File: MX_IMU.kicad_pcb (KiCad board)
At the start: 4 copper layers, 40 x 36 mm, 50 parts, among them J1 CAN, J2 USART, J401 SWD, SW1 SW_SPST, U1 ld39150dt33-r, U2 ICM-42688-P, U200 STM32F405RGT6, U4 AT24C256, U6 TJA1051T/3, Y200 16MHz

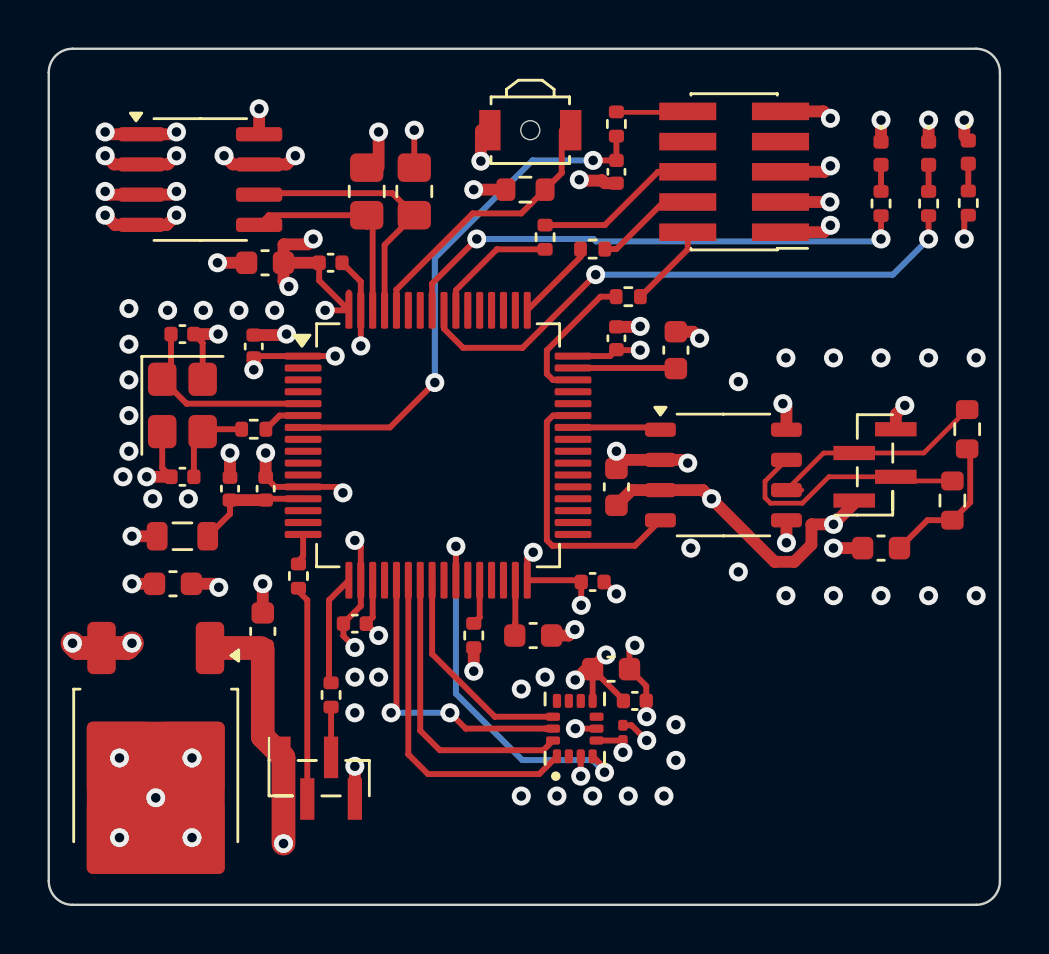
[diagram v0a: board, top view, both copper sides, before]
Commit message: add usb and clean up
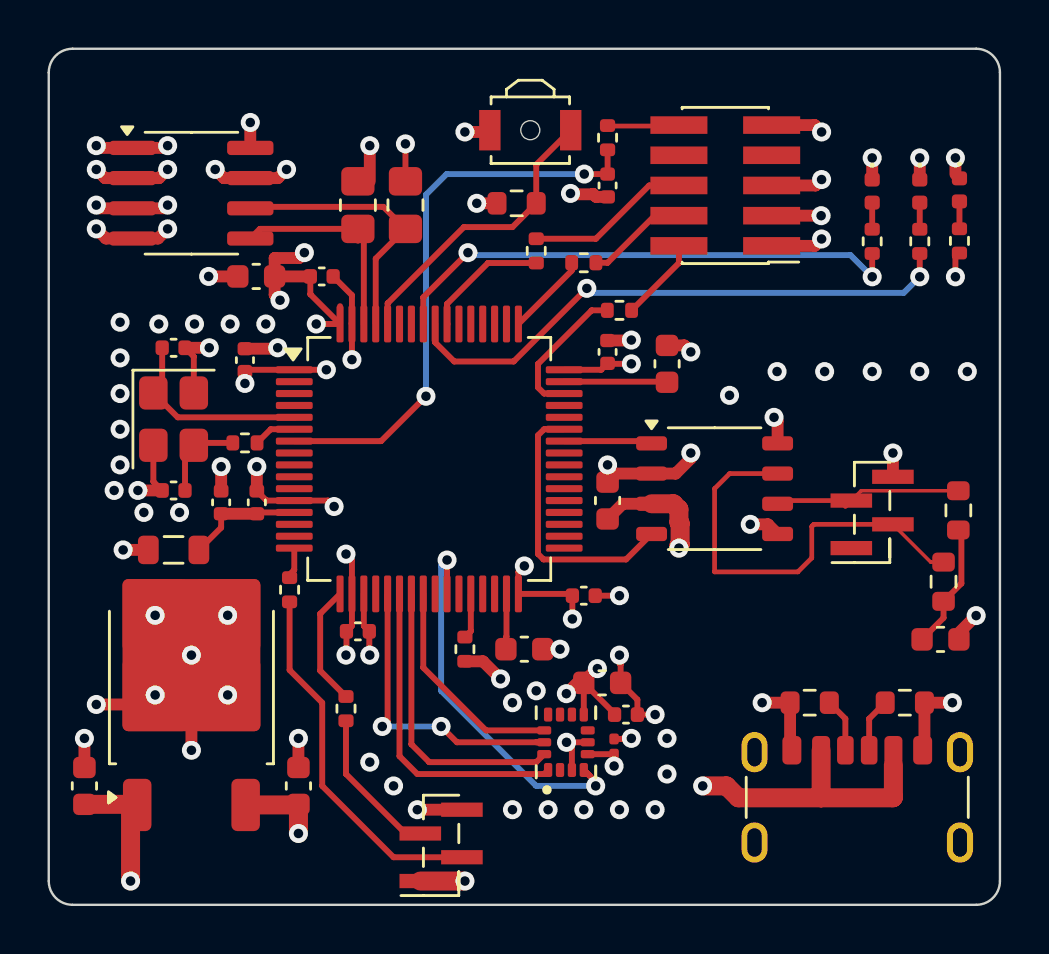
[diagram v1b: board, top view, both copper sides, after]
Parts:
- added J3: 2171750001, common:molex_2171750001_usb_c_6p, F.Cu at (156.1, 118.9)
- added R1: 5k1, Resistor_SMD:R_0603_1608Metric, F.Cu at (158.1, 113.8)
- added R2: 5k1, Resistor_SMD:R_0603_1608Metric, F.Cu at (154.1, 113.8)
- moved C4 10.0 mm to (132.6, 117.3), turned to 90 degrees
- moved C3 9.92 mm to (123.6, 117.3)
- moved J2 5.85 mm to (138.6, 119.8), turned to 180 degrees
- moved C31 4.58 mm to (159.6, 111.2), turned to 0 degrees
- moved U1 3.79 mm to (128.1, 113.1), turned to 90 degrees
- moved R19 3.43 mm to (160.3, 105.7)
- moved R20 3.43 mm to (159.7, 108.7)
- moved J1 2.00 mm to (156.7, 105.8)
- moved D5 1.63 mm to (160.3, 92.3)
- moved R29 1.63 mm to (160.3, 94.4)
- moved D3 1.63 mm to (158.7, 92.3)
- moved D4 1.63 mm to (156.7, 92.3)
- moved R13 1.63 mm to (158.7, 94.4)
- moved R14 1.63 mm to (156.7, 94.4)
- moved R407 0.85 mm to (134.6, 114.1)
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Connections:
- J1 pad 1: +5V -> unconnected-(J1-Pin_1-Pad1)
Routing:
- net GND: track 74.3 -> 90.6 mm, vias 51 -> 54
- net /Connectors/CAN1+: track 10.5 -> 18.3 mm
- net Net-(J2-Pin_2): track 9.07 -> 15.4 mm
- net Net-(J2-Pin_3): track 2.11 -> 6.40 mm
- net +5V: track 26.9 -> 24.6 mm
- net Net-(J3-CC2): track 0.00 -> 2.28 mm
- net Net-(J3-CC1): track 0.00 -> 2.28 mm
- net NRST: track 22.1 -> 24.0 mm
- net /Connectors/CAN1-: track 9.65 -> 8.18 mm
- net BOOT0: track 11.7 -> 12.5 mm
- net GYRO_MISO: track 14.2 -> 13.5 mm
- net Net-(C31-Pad1): track 6.08 -> 5.34 mm
- net +3.3V: track 44.5 -> 44.8 mm, vias 23 -> 21
- net (no net): vias 36 -> 29

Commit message: add mounting hole
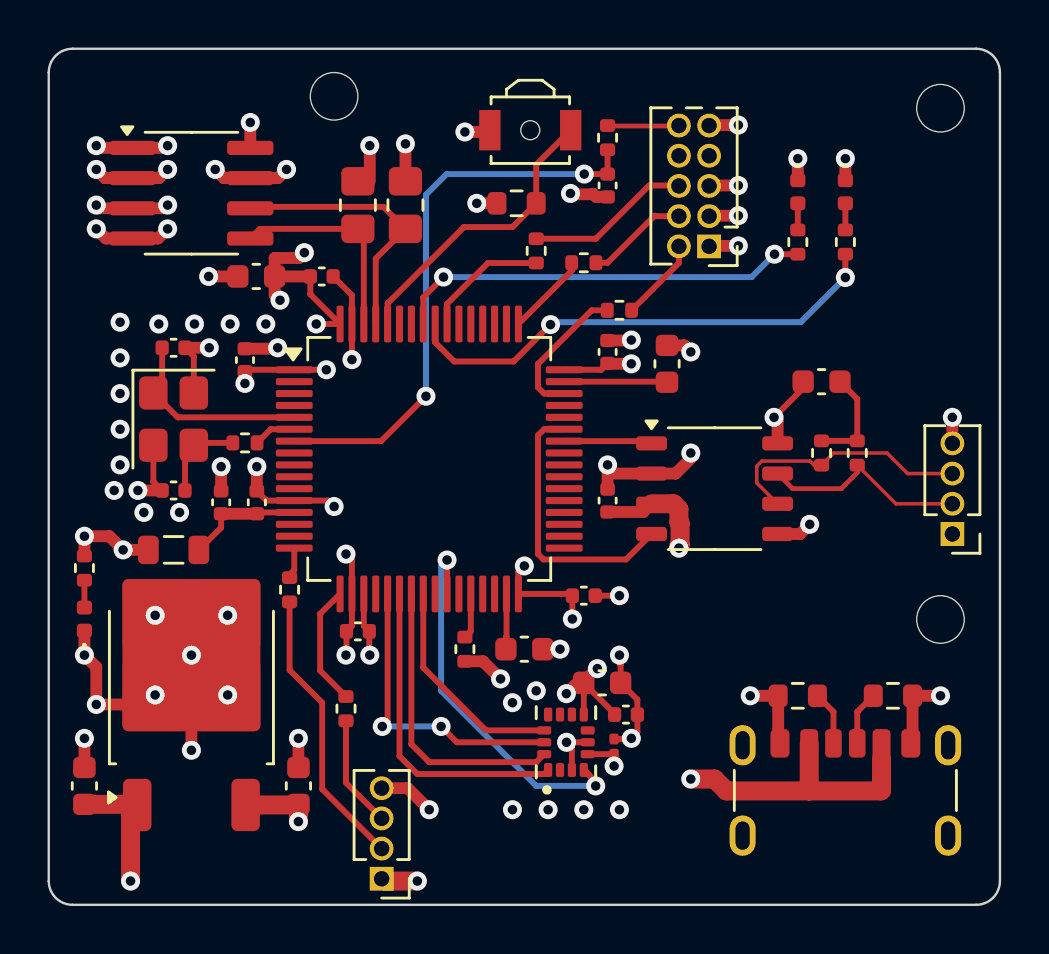
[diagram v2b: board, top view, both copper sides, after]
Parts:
- removed C29: 100n, Capacitor_SMD:C_0603_1608Metric
- removed C7: 2u2, Capacitor_SMD:C_0603_1608Metric
- added C2: 100n, Capacitor_SMD:C_0402_1005Metric, F.Cu at (145.6, 105.3)
- added C5: 2u2, Capacitor_SMD:C_0603_1608Metric, F.Cu at (132.6, 117.3)
- added H1: MountingHole, MountingHole:MountingHole_2mm, F.Cu at (159.6, 88.8)
- added H2: MountingHole, MountingHole:MountingHole_2mm, F.Cu at (134.1, 88.3)
- added H3: MountingHole, MountingHole:MountingHole_2mm, F.Cu at (159.6, 110.3)
- J1: value CAN -> pinheader; footprint Connector_PinHeader_1.00mm:PinHeader_1x04_P1.00mm_Vertical_SMD_Pin1Right -> Connector_PinHeader_1.27mm:PinHeader_1x04_P1.27mm_Vertical
- J2: value USART -> pinheader; footprint Connector_PinHeader_1.00mm:PinHeader_1x04_P1.00mm_Vertical_SMD_Pin1Right -> Connector_PinHeader_1.27mm:PinHeader_1x04_P1.27mm_Vertical
- J401: footprint Connector_PinHeader_1.27mm:PinHeader_2x05_P1.27mm_Vertical_SMD -> Connector_PinHeader_1.27mm:PinHeader_2x05_P1.27mm_Vertical
- R19, R20: footprint Resistor_SMD:R_0603_1608Metric -> Resistor_SMD:R_0402_1005Metric
- moved D5 41.0 mm to (123.6, 110.3), turned to 90 degrees
- moved R29 39.3 mm to (123.6, 108.2), turned to -90 degrees
- moved C4 13.5 mm to (145.3, 113.0), turned to 0 degrees
- moved C31 11.9 mm to (154.6, 100.3), turned to 180 degrees
- moved R20 6.52 mm to (156.1, 103.3), turned to 90 degrees
- moved R19 6.24 mm to (154.6, 103.3), turned to 90 degrees
- moved J1 3.49 mm to (160.1, 106.7)
- moved D3 3.13 mm to (155.6, 92.3)
- moved D4 3.13 mm to (153.6, 92.3)
- moved R13 3.13 mm to (155.6, 94.5)
- moved R14 3.13 mm to (153.6, 94.5)
- moved J2 2.87 mm to (136.1, 121.2)
- moved J401 2.65 mm to (149.8, 94.6)
- moved J3 0.58 mm to (155.6, 118.6)
- moved R1 0.58 mm to (157.6, 113.5)
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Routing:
- net /Connectors/CAN1+: track 18.3 -> 8.88 mm
- net STATUS_LED2: track 22.2 -> 17.6 mm
- net Net-(J2-Pin_2): track 15.4 -> 12.0 mm
- net STATUS_LED1: track 24.1 -> 20.8 mm
- net GND: track 90.6 -> 87.8 mm, vias 54 -> 52
- net /Connectors/CAN1-: track 8.18 -> 10.9 mm
- net +3.3V: track 44.8 -> 42.8 mm
- net Net-(J2-Pin_3): track 6.40 -> 4.73 mm
- net EEPROM_SDA: track 9.88 -> 8.44 mm
- net Net-(C31-Pad1): track 5.34 -> 4.29 mm
- net Net-(C211-Pad1): track 3.73 -> 3.07 mm
- net +5V: track 24.6 -> 23.9 mm
- net HSE_IN: track 8.40 -> 7.88 mm
- net (no net): vias 29 -> 18

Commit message: Cleanup and check on JCLPCB
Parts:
- removed J401: SWD, Connector_PinHeader_1.27mm:PinHeader_2x05_P1.27mm_Vertical
- removed R402: 22, Resistor_SMD:R_0402_1005Metric
- added J4: ZX-PZ2.54-1-5PZZ, CONN-HEADER-VERT-5POS-2.54MM:CONN-HEADER-VERT-5POS-2.54MM, F.Cu at (155.1, 96.3)
- J1, J2: value pinheader -> KH-1.27PH180-1X4P-L7.2
- R19, R20: footprint Resistor_SMD:R_0402_1005Metric -> Resistor_SMD:R_0603_1608Metric
- moved R403 14.9 mm to (157.6, 98.8), turned to 0 degrees
- moved C400 12.2 mm to (155.6, 99.1)
- moved D4 10.3 mm to (143.6, 89.8)
- moved R14 10.3 mm to (143.6, 91.9)
- moved D3 10.3 mm to (145.6, 89.8)
- moved R13 10.3 mm to (145.6, 92.0)
- moved H2 9.51 mm to (124.6, 88.8)
- moved R400 6.33 mm to (152.1, 99.3)
- moved R401 2.50 mm to (146.1, 97.3)
- moved SW1 2.29 mm to (140.0, 89.5), turned to -90 degrees
- moved U4 2.28 mm to (130.3, 92.4)
- moved R9 2.01 mm to (139.7, 93.0), turned to 0 degrees
- moved C31 0.50 mm to (154.6, 100.8)
- moved R20 0.50 mm to (156.6, 103.3)
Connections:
- U200 pad 55: SWO -> unconnected-(U200-PB3-Pad55)
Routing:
- net STATUS_LED1: track 20.8 -> 10.8 mm, vias 2 -> 0
- net STATUS_LED2: track 17.6 -> 9.19 mm, vias 2 -> 0
- net Net-(J401-Pin_6): track 6.93 -> 0.00 mm
- net GND: track 87.8 -> 81.4 mm, vias 52 -> 48
- net SWO: track 5.31 -> 0.00 mm
- net BOOT0: track 12.5 -> 8.27 mm
- net Net-(J4-Pad3): track 0.00 -> 3.54 mm
- net NRST: track 23.8 -> 26.5 mm
- net SWDIO: track 6.04 -> 8.65 mm
- net EEPROM_SDA: track 8.44 -> 6.16 mm
- net EEPROM_SCL: track 11.4 -> 9.08 mm
- net +3.3V: track 42.8 -> 41.2 mm, vias 21 -> 20
- net +5V: track 23.9 -> 24.9 mm
- net Net-(J4-Pad2): track 3.53 -> 2.94 mm
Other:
- board text added: "IMU_Ver_1.0 by MX Motion Canada Day"
